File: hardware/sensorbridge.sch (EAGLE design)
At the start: 23 parts

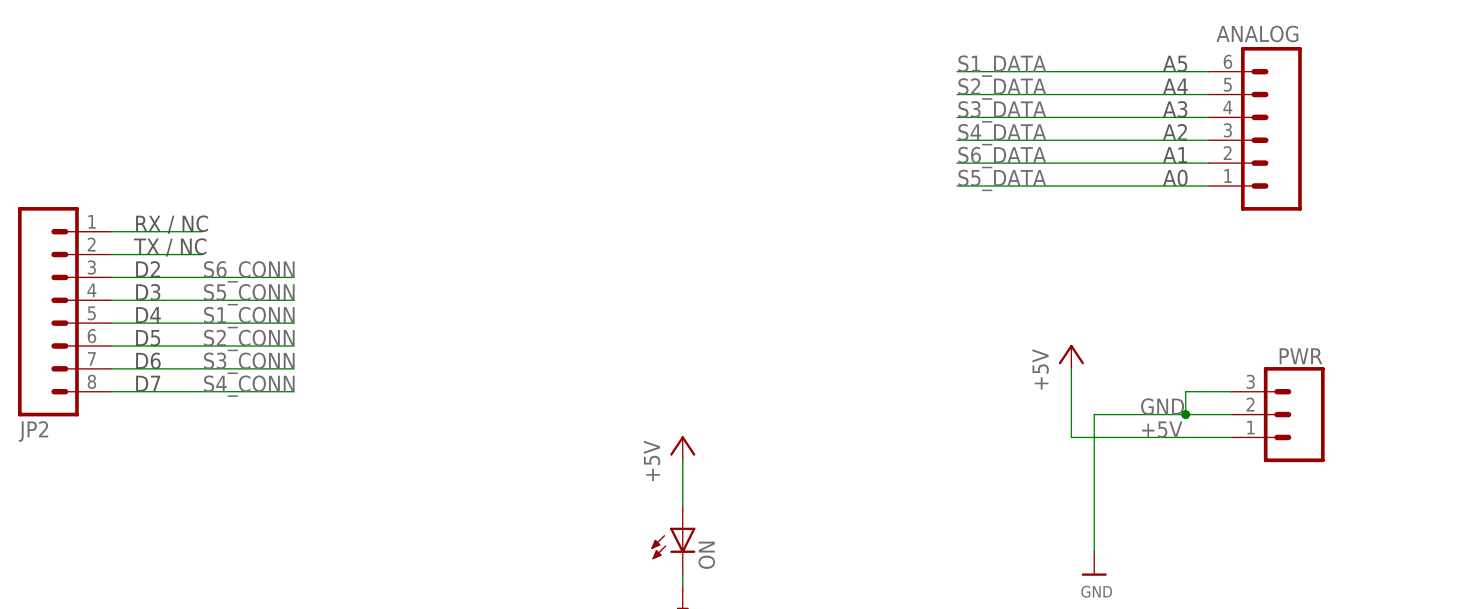
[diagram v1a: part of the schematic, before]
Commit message: Replaced connectors with no-silk versions
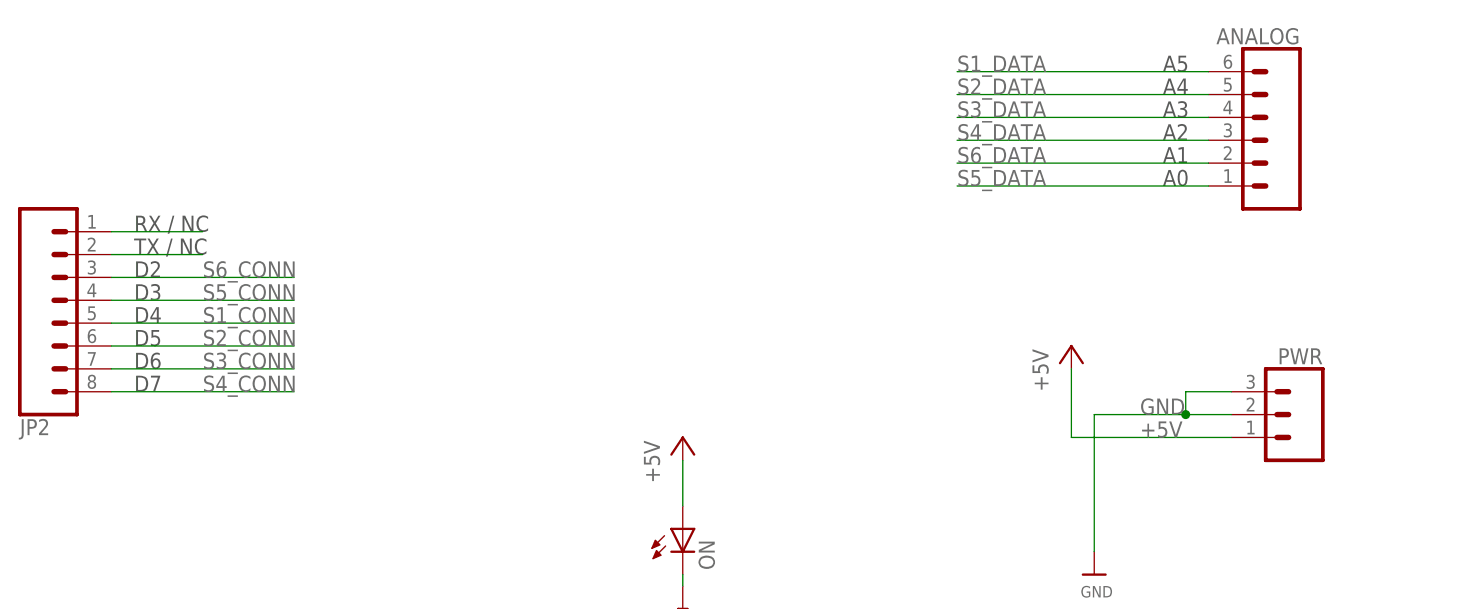
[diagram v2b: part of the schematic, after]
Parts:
- ANALOG: device SparkFun-Connectors:M06SILK_FEMALE_PTH -> SparkFun-Connectors:CONN_06NO_SILK_FEMALE_PTH
- JP2: device SparkFun-Connectors:M08 -> SparkFun-Connectors:CONN_08NO_SILK_FEMALE_PTH
- PWR: device SparkFun-Connectors:CONN_03 -> SparkFun-Connectors:CONN_031X03_NO_SILK
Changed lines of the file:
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@@
 <grid distance="0.1" unitdist="inch" unit="inch" style="lines" multiple="1" display="no" altdistance="0.01" altunitdist="inch" altunit="inch"/>
 <layers>
-<layer number="1" name="Top" color="4" fill="1" visible="no" active="no"/>
-<layer number="16" name="Bottom" color="1" fill="1" visible="no" active="no"/>
-<layer number="17" name="Pads" color="2" fill="1" visible="no" active="no"/>
-<layer number="18" name="Vias" color="2" fill="1" visible="no" active="no"/>
-<layer number="19" name="Unrouted" color="6" fill="1" visible="no" active="no"/>
-<layer number="20" name="Dimension" color="15" fill="1" visible="no" active="no"/>
-<layer number="21" name="tPlace" color="7" fill="1" visible="no" active="no"/>
-<layer number="22" name="bPlace" color="7" fill="1" visible="no" active="no"/>
-<layer number="23" name="tOrigins" color="15" fill="1" visible="no" active="no"/>
-<layer number="24" name="bOrigins" color="15" fill="1" visible="no" active="no"/>
-<layer number="25" name="tNames" color="7" fill="1" visible="no" active="no"/>
-<layer number="26" name="bNames" color="7" fill="1" visible="no" active="no"/>
-<layer number="27" name="tValues" color="7" fill="1" visible="no" active="no"/>
-<layer number="28" name="bValues" color="7" fill="1" visible="no" active="no"/>
+<layer number="1" name="Top" color="4" fill="1" visible="yes" active="no"/>
+<layer number="16" name="Bottom" color="1" fill="1" visible="yes" active="no"/>
+<layer number="17" name="Pads" color="2" fill="1" visible="yes" active="no"/>
+<layer number="18" name="Vias" color="2" fill="1" visible="yes" active="no"/>
+<layer number="19" name="Unrouted" color="6" fill="1" visible="yes" active="no"/>
+<layer number="20" name="Dimension" color="15" fill="1" visible="yes" active="no"/>
+<layer number="21" name="tPlace" color="7" fill="1" visible="yes" active="no"/>
+<layer number="22" name="bPlace" color="7" fill="1" visible="yes" active="no"/>
+<layer number="23" name="tOrigins" color="15" fill="1" visible="yes" active="no"/>
+<layer number="24" name="bOrigins" color="15" fill="1" visible="yes" active="no"/>
+<layer number="25" name="tNames" color="7" fill="1" visible="yes" active="no"/>
+<layer number="26" name="bNames" color="7" fill="1" visible="yes" active="no"/>
+<layer number="27" name="tValues" color="7" fill="1" visible="yes" active="no"/>
+<layer number="28" name="bValues" color="7" fill="1" visible="yes" active="no"/>
 <layer number="29" name="tStop" color="7" fill="3" visible="no" active="no"/>
 <layer number="30" name="bStop" color="7" fill="6" visible="no" active="no"/>
@@
 <layer number="35" name="tGlue" color="7" fill="4" visible="no" active="no"/>
 <layer number="36" name="bGlue" color="7" fill="5" visible="no" active="no"/>
-<layer number="37" name="tTest" color="7" fill="1" visible="no" active="no"/>
-<layer number="38" name="bTest" color="7" fill="1" visible="no" active="no"/>
+<layer number="37" name="tTest" color="7" fill="1" visible="yes" active="no"/>
+<layer number="38" name="bTest" color="7" fill="1" visible="yes" active="no"/>
 <layer number="39" name="tKeepout" color="4" fill="11" visible="no" active="no"/>
 <layer number="40" name="bKeepout" color="1" fill="11" visible="no" active="no"/>
@@
 <layer number="44" name="Drills" color="7" fill="1" visible="no" active="no"/>
 <layer number="45" name="Holes" color="7" fill="1" visible="no" active="no"/>
-<layer number="46" name="Milling" color="3" fill="1" visible="no" active="no"/>
-<layer number="47" name="Measures" color="7" fill="1" visible="no" active="no"/>
-<layer number="48" name="Document" color="7" fill="1" visible="no" active="no"/>
-<layer number="49" name="Reference" color="7" fill="1" visible="no" active="no"/>
-<layer number="50" name="dxf" color="7" fill="1" visible="no" active="no"/>
-<layer number="51" name="tDocu" color="7" fill="1" visible="no" active="no"/>
-<layer number="52" name="bDocu" color="7" fill="1" visible="no" active="no"/>
-<layer number="53" name="tGND_GNDA" color="7" fill="9" visible="no" active="no"/>
-<layer number="54" name="bGND_GNDA" color="1" fill="9" visible="no" active="no"/>
-<layer number="56" name="wert" color="7" fill="1" visible="no" active="no"/>
-<layer number="57" name="tCAD" color="7" fill="1" visible="no" active="no"/>
-<layer number="59" name="tCarbon" color="7" fill="1" visible="no" active="no"/>
-<layer number="60" name="bCarbon" color="7" fill="1" visible="no" active="no"/>
+<layer number="46" name="Milling" color="3" fill="1" visible="yes" active="no"/>
+<layer number="47" name="Measures" color="7" fill="1" visible="yes" active="no"/>
+<layer number="48" name="Document" color="7" fill="1" visible="yes" active="no"/>
+<layer number="49" name="Reference" color="7" fill="1" visible="yes" active="no"/>
+<layer number="50" name="dxf" color="7" fill="1" visible="yes" active="no"/>
+<layer number="51" name="tDocu" color="7" fill="1" visible="yes" active="no"/>
+<layer number="52" name="bDocu" color="7" fill="1" visible="yes" active="no"/>
+<layer number="53" name="tGND_GNDA" color="7" fill="9" visible="yes" active="no"/>
+<layer number="54" name="bGND_GNDA" color="1" fill="9" visible="yes" active="no"/>
+<layer number="56" name="wert" color="7" fill="1" visible="yes" active="no"/>
+<layer number="57" name="tCAD" color="7" fill="1" visible="yes" active="no"/>
+<layer number="59" name="tCarbon" color="7" fill="1" visible="yes" active="no"/>
+<layer number="60" name="bCarbon" color="7" fill="1" visible="yes" active="no"/>
 <layer number="90" name="Modules" color="5" fill="1" visible="yes" active="yes"/>
 <layer number="91" name="Nets" color="2" fill="1" visible="yes" active="yes"/>
@@
 <part name="P+7" library="supply1" deviceset="+5V" device=""/>
 <part name="U$14" library="microbuilder" deviceset="GND" device=""/>
-<part name="ANALOG" library="SparkFun-Connectors" deviceset="M06" device="SILK_FEMALE_PTH"/>
-<part name="JP2" library="SparkFun-Connectors" deviceset="M08" device=""/>
+<part name="ANALOG" library="SparkFun-Connectors" deviceset="CONN_06" device="NO_SILK_FEMALE_PTH"/>
+<part name="JP2" library="SparkFun-Connectors" deviceset="CONN_08" device="NO_SILK_FEMALE_PTH"/>
 <part name="ON" library="adafruit" deviceset="LED" device="CHIP-LED0603"/>
 <part name="R8" library="Seeed-OPL-Resistor" deviceset="RES" device="-0603"/>
 <part name="U$15" library="microbuilder" deviceset="GND" device=""/>
 <part name="P+8" library="supply1" deviceset="+5V" device=""/>
-<part name="PWR" library="SparkFun-Connectors" deviceset="CONN_03" device=""/>
+<part name="PWR" library="SparkFun-Connectors" deviceset="CONN_03" device="1X03_NO_SILK"/>
 </parts>
 <sheets>

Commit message: Changed connectors, made LED pin-controlled
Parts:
- removed INPUT1, INPUT2, INPUT3, INPUT4, INPUT5, INPUT6: MJ-2135, sensorlab:MJ-2135
- removed LED4, LED5, LED6: (no value), adafruit:LEDCHIP-LED0603
- removed R4, R5, R6: (no value), Seeed-OPL-Resistor:RES-0603
- added INPUT_1, INPUT_2, INPUT_3: S5B-PH-K-S(LF)(SN), S5B-PH-K-S_LF__SN_:S5B-PH-K-S(LF)(SN)
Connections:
- removed net N$4: LED4.C, R4.2
- removed net N$5: LED5.C, R5.2
- removed net N$6: LED6.C, R6.2
- removed net S4_CONN: INPUT4.3, JP2.8, LED4.A
- removed net S4_DATA: ANALOG.3, INPUT4.2
- removed net S5_CONN: INPUT5.3, JP2.4, LED5.A
- removed net S5_DATA: ANALOG.1, INPUT5.2
- removed net S6_CONN: INPUT6.3, JP2.3, LED6.A
- removed net S6_DATA: ANALOG.2, INPUT6.2
- new net S1_LED: JP2.6, LED1.A
- new net S2_LED: JP2.7, LED2.A
- new net S3_LED: JP2.8, LED3.A
- net +5V: now also INPUT_1.4, INPUT_1.5, INPUT_2.4, INPUT_2.5, INPUT_3.4, INPUT_3.5; no longer INPUT1.4, INPUT2.4, INPUT3.4, INPUT4.4, INPUT5.4, INPUT6.4
- net GND: now also INPUT_1.1, INPUT_2.1, INPUT_3.1; no longer INPUT1.1, INPUT2.1, INPUT3.1, INPUT4.1, INPUT5.1, INPUT6.1, R4.1, R5.1, R6.1
- net S1_CONN: now also INPUT_1.3, JP2.3; no longer INPUT1.3, JP2.5, LED1.A
- net S1_DATA: now also INPUT_1.2; no longer INPUT1.2
- net S2_CONN: now also INPUT_2.3, JP2.4; no longer INPUT2.3, JP2.6, LED2.A
- net S2_DATA: now also INPUT_2.2; no longer INPUT2.2
- net S3_CONN: now also INPUT_3.3, JP2.5; no longer INPUT3.3, JP2.7, LED3.A
- net S3_DATA: now also INPUT_3.2; no longer INPUT3.2
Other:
- moved on the sheet: LED1, LED2, LED3, R1, R2, R3

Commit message: Made sensor connection through GND instead of VCC, added pulldown resistors to DATA lines
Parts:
- added R4, R5, R6: 10K, Seeed-OPL-Resistor:RES-0603
- R1, R2, R3, R8: value (none) -> 470
- renumbered ANALOG to ARDUINO_ANALOG, JP2 to ARDUINO_DIGITAL, PWR to ARDUINO_SUPPLY
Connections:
- net +5V: no longer INPUT_1.4, INPUT_2.4, INPUT_3.4
- net GND: now also INPUT_1.4, INPUT_2.4, INPUT_3.4, R4.1, R5.1, R6.1
- net S1_DATA: now also R4.2
- net S2_DATA: now also R5.2
- net S3_DATA: now also R6.2
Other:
- note added: "Connected by wire to ground"
